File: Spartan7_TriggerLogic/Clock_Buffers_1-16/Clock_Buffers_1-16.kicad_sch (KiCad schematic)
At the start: 38 parts, among them J1 Out_1, J10 Out_10, J11 Out_11, J12 Out_12, J13 Out_13, J14 Out_14, J15 Out_15, J16 Out_16, J17 CLK_In, J2 Out_2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

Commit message: .
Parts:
- added D101: 5V, LED_SMD:LED_0603_1608Metric, symbol Device:LED
- added D102: 3V3, LED_SMD:LED_0603_1608Metric, symbol Device:LED
- added H1, H2, H3, H4: fi_2.6mm, MountingHole:MountingHole_2.7mm_M2.5_Pad_Via, symbol Mechanical:MountingHole_Pad
- added J18: USB_C_Receptacle_PowerOnly_6P, 0_lib:CONN6_USB4125_GCT, symbol Connector:USB_C_Receptacle_PowerOnly_6P
- added J19: Soldarable pads, Connector_PinHeader_2.00mm:PinHeader_1x02_P2.00mm_Horizontal, symbol Connector:Conn_01x02_Socket
- added R101, R102, R19, R20: 5k1, Resistor_SMD:R_0402_1005Metric, symbol Device:R
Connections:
- net +3V3: now also R102.1
- net GND: now also D101.1 (K), D102.1 (K), H1.1, H2.1, H3.1, H4.1, J18.A12 (GND), J18.B12 (GND), J18.S1 (SHIELD), J19.1 (Pin_1), R19.2, R20.2
- net out_1: now also J3.1 (In); no longer J1.1 (In)
- net out_10: now also J11.1 (In); no longer J10.1 (In)
- net out_11: now also J4.1 (In); no longer J11.1 (In)
- net out_12: now also J5.1 (In); no longer J12.1 (In)
- net out_13: now also J14.1 (In); no longer J13.1 (In)
- net out_14: now also J8.1 (In); no longer J14.1 (In)
- net out_16: now also J7.1 (In); no longer J16.1 (In)
- net out_2: now also J9.1 (In); no longer J2.1 (In)
- net out_3: now also J16.1 (In); no longer J3.1 (In)
- net out_4: now also J13.1 (In); no longer J4.1 (In)
- net out_5: now also J2.1 (In); no longer J5.1 (In)
- net out_6: now also J12.1 (In); no longer J6.1 (In)
- net out_7: now also J6.1 (In); no longer J7.1 (In)
- net out_8: now also J1.1 (In); no longer J8.1 (In)
- net out_9: now also J10.1 (In); no longer J9.1 (In)
- new net: J18.A5 (CC1), R20.1
- new net: D102.2 (A), R102.2
- new net: J18.B5 (CC2), R19.1
- new net: D101.2 (A), R101.2
- new net 5V_to_3V3/V_in: J18.A9 (VBUS), J18.B9 (VBUS), J19.2 (Pin_2), R101.1
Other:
- added sheet 5V_to_3V3 (LT3081EDF.kicad_sch)

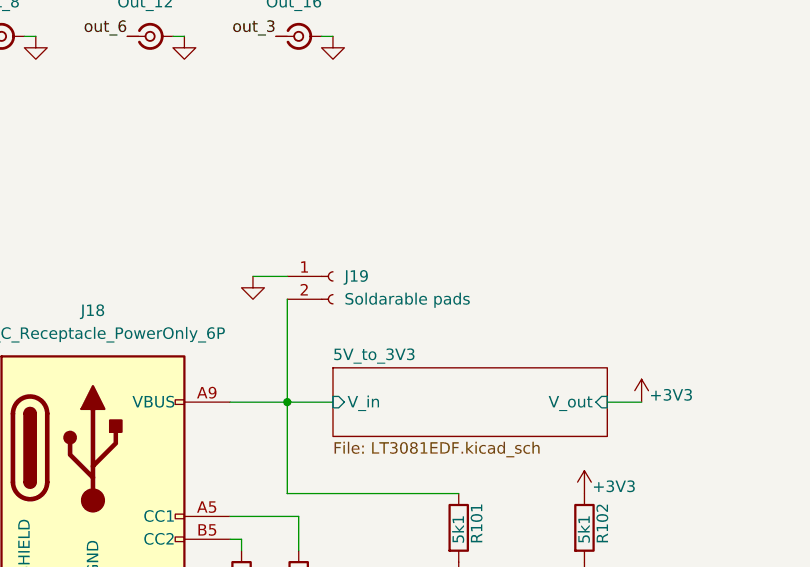
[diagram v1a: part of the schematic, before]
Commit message: Update PCB layout and add new backup and SPICE files
Added new backup ZIP files and SPICE simulation files for Clock_Buffers_1-16 and HYDRA_VMM3_CARD_V3_Flex, while removing outdated backup files. Updated multiple footprints and component placements in Clock_Buffers_1-16.kicad_pcb, reflecting changes in component positions and orientations. Minor update to .kicad_prl files to reflect active layer changes.
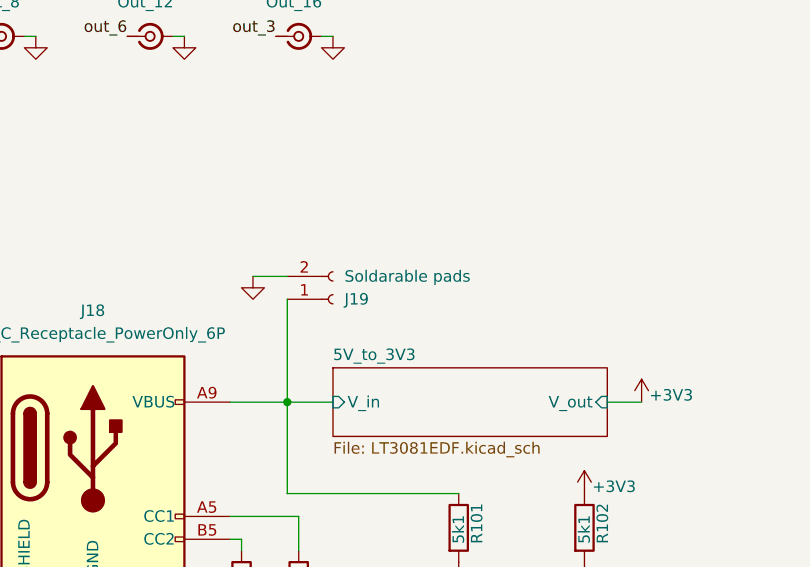
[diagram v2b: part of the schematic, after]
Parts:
- J19: footprint Connector_PinHeader_2.00mm:PinHeader_1x02_P2.00mm_Horizontal -> Connector_JST:JST_PH_S2B-PH-K_1x02_P2.00mm_Horizontal
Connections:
- net 5V_to_3V3/V_in: now also J19.1 (Pin_1); no longer J19.2 (Pin_2)
- net GND: now also J19.2 (Pin_2); no longer J19.1 (Pin_1)
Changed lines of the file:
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@@
 	(wire
 		(pts
-			(xy 163.83 31.75) (xy 162.56 31.75)
+			(xy 204.47 101.6) (xy 208.28 101.6)
 		)
 		(stroke
@@
 	(wire
 		(pts
-			(xy 204.47 101.6) (xy 208.28 101.6)
+			(xy 163.83 31.75) (xy 162.56 31.75)
 		)
 		(stroke
@@
 	(symbol
 		(lib_id "Connector:Conn_01x02_Socket")
-		(at 213.36 101.6 0)
+		(at 213.36 104.14 0)
+		(mirror x)
 		(unit 1)
 		(exclude_from_sim no)
@@
 		(on_board yes)
 		(dnp no)
-		(fields_autoplaced yes)
 		(property "Reference" "J19"
-			(at 214.63 101.5999 0)
+			(at 214.63 104.1401 0)
 			(effects
 				(font
@@
 		)
 		(property "Value" "Soldarable pads"
-			(at 214.63 104.1399 0)
+			(at 214.63 101.6001 0)
 			(effects
 				(font
@@
 			)
 		)
-		(property "Footprint" "Connector_PinHeader_2.00mm:PinHeader_1x02_P2.00mm_Horizontal"
-			(at 213.36 101.6 0)
+		(property "Footprint" "Connector_JST:JST_PH_S2B-PH-K_1x02_P2.00mm_Horizontal"
+			(at 213.36 104.14 0)
 			(effects
 				(font
@@
 		)
 		(property "Datasheet" "~"
-			(at 213.36 101.6 0)
+			(at 213.36 104.14 0)
 			(effects
 				(font
@@
 		)
 		(property "Description" "Generic connector, single row, 01x02, script generated"
-			(at 213.36 101.6 0)
+			(at 213.36 104.14 0)
 			(effects
 				(font
